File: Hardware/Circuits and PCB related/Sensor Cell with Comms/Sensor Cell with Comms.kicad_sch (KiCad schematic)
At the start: 27 parts, among them J1 MolexMicroFit3_1, J2 MolexMicroFit3_2, J3 MolexMicroFit3_3, U1 STM32F103C6T6

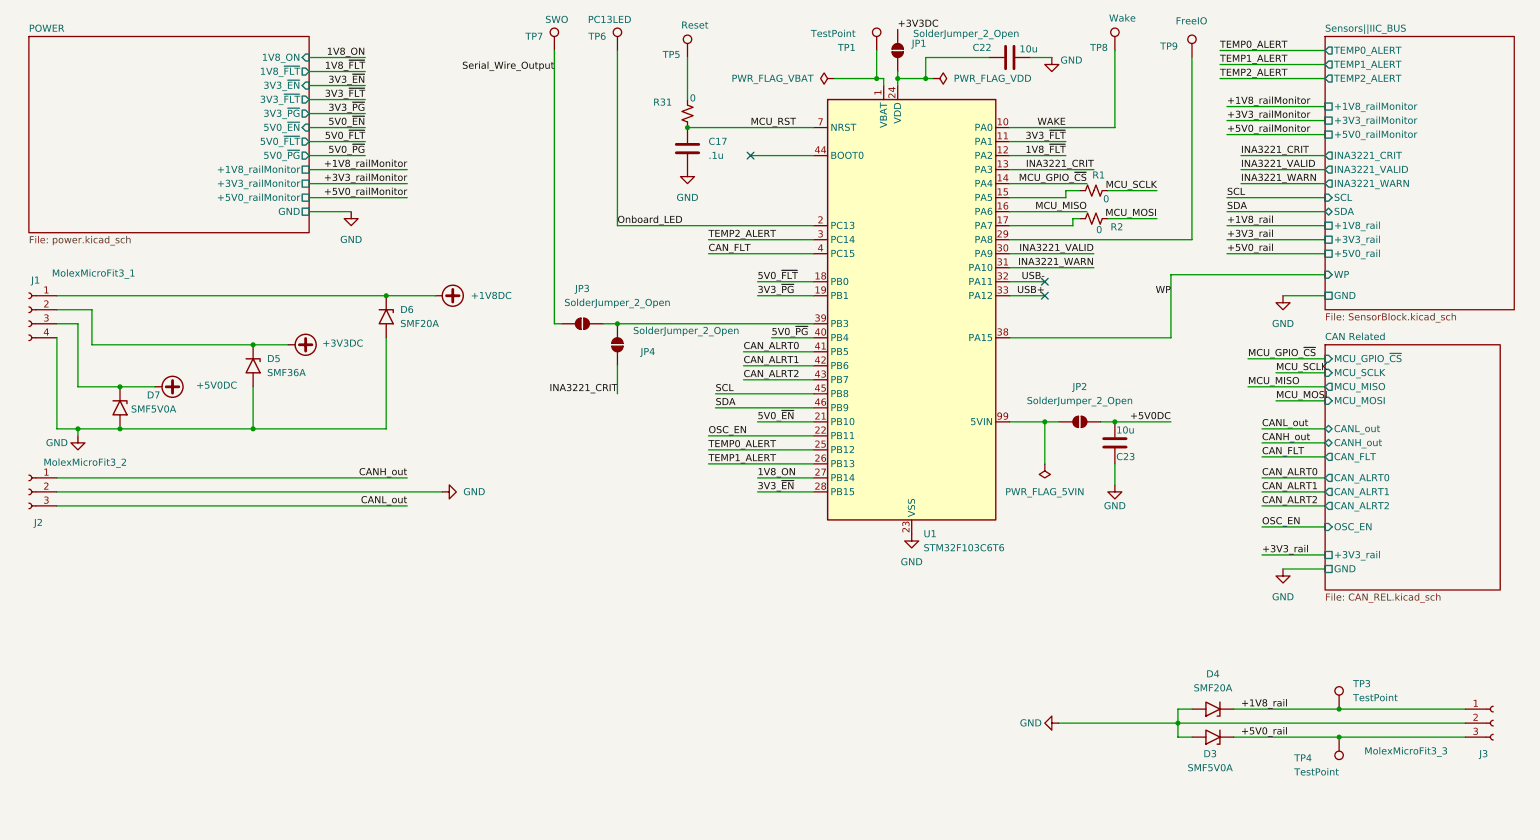
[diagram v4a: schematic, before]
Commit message: Rev2 PCB finished, need to document and catalog for Iowa Innovation challenge this thursday
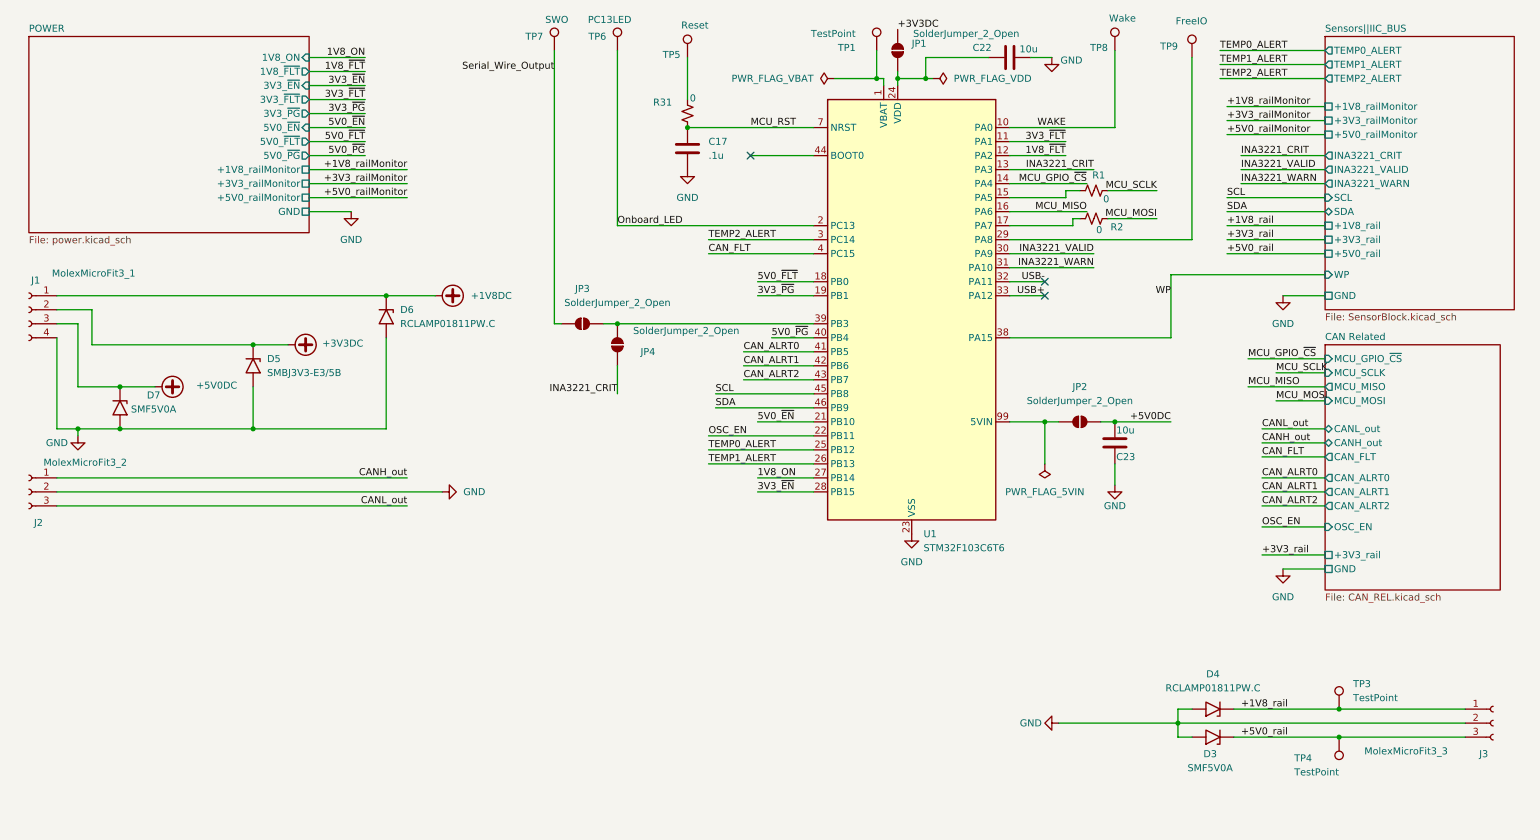
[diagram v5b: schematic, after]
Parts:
- D4, D6: value SMF20A -> RCLAMP01811PW.C
- D5: value SMF36A -> SMBJ3V3-E3/5B
- J2: footprint Connector_Molex:Molex_Micro-Latch_53254-0370_1x03_P2.00mm_Horizontal -> footprintLib:CONN_SD-43650-001_03_MOL
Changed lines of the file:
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@@
 			)
 		)
-		(property "Value" "SMF20A"
+		(property "Value" "RCLAMP01811PW.C"
 			(at 229.87 134.62 0)
 			(effects
@@
 			)
 		)
-		(property "Value" "SMF36A"
+		(property "Value" "SMBJ3V3-E3/5B"
 			(at 58.42 77.4699 90)
 			(effects
@@
 			)
 		)
-		(property "Footprint" "Connector_Molex:Molex_Micro-Latch_53254-0370_1x03_P2.00mm_Horizontal"
+		(property "Footprint" "footprintLib:CONN_SD-43650-001_03_MOL"
 			(at 15.24 99.06 0)
 			(effects
@@
 			)
 		)
-		(property "Value" "SMF20A"
+		(property "Value" "RCLAMP01811PW.C"
 			(at 82.55 68.5799 90)
 			(effects
